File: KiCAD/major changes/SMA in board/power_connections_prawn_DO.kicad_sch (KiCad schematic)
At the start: 15 parts, among them IC1 74LVT245D,118, IC2 74LVT245D,118, IC3 74LVT245D,118, IC4 74LVT245D,118

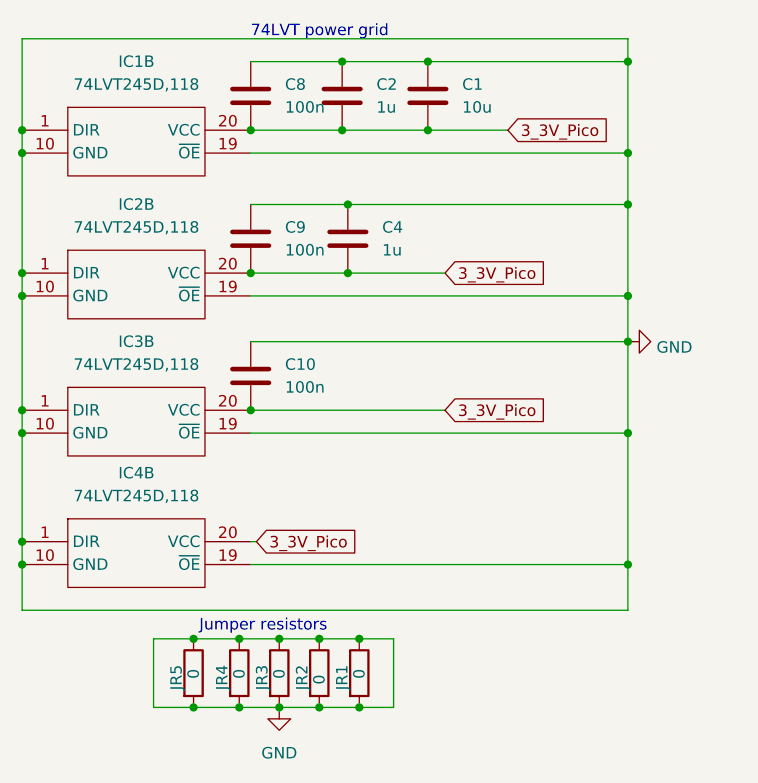
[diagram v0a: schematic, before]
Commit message: Added Mounting holes to board
Mounting holes line up with Prawnblaster.

Changed layout of components to make spacing better
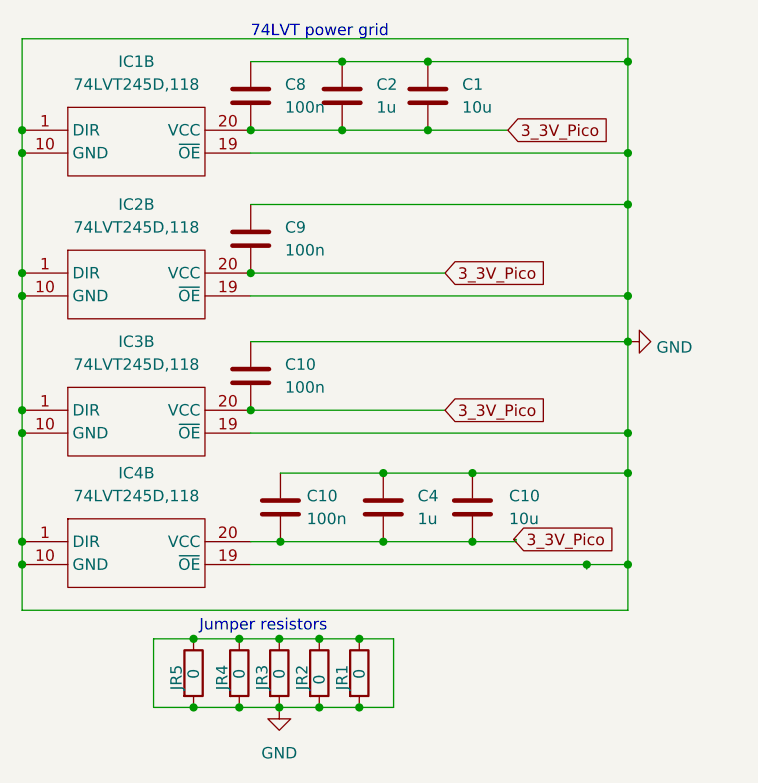
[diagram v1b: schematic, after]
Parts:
- added C10: 10u, Capacitor_SMD:C_0805_2012Metric_Pad1.18x1.45mm_HandSolder, symbol Device:C
- added C10: 100n, Capacitor_SMD:C_0805_2012Metric_Pad1.18x1.45mm_HandSolder, symbol Device:C
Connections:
- net 3_3V_Pico: now also C10.2, C10.2
- net GND: now also C10.1, C10.1
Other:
- moved on the sheet: C4
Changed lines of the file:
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@@
   (junction (at 51.435 89.535) (diameter 0) (color 0 0 0 0)
   )
-  (junction (at 59.055 41.275) (diameter 0) (color 0 0 0 0)
+  (junction (at 72.898 63.5) (diameter 0) (color 0 0 0 0)
   )
   (junction (at 67.945 17.78) (diameter 0) (color 0 0 0 0)
@@
   (junction (at 46.99 89.535) (diameter 0) (color 0 0 0 0)
   )
+  (junction (at 51.562 71.12) (diameter 0) (color 0 0 0 0)
+  )
+  (junction (at 62.992 63.5) (diameter 0) (color 0 0 0 0)
+  )
+  (junction (at 85.598 73.66) (diameter 0) (color 0 0 0 0)
+  )
   (junction (at 46.99 81.915) (diameter 0) (color 0 0 0 0)
   )
@@
   (junction (at 22.86 56.515) (diameter 0) (color 0 0 0 0)
   )
-  (junction (at 59.055 33.655) (diameter 0) (color 0 0 0 0)
-  )
   (junction (at 55.88 89.535) (diameter 0) (color 0 0 0 0)
   )
@@
   (junction (at 22.86 25.4) (diameter 0) (color 0 0 0 0)
   )
+  (junction (at 72.898 71.12) (diameter 0) (color 0 0 0 0)
+  )
   (junction (at 22.86 73.66) (diameter 0) (color 0 0 0 0)
   )
@@
   (junction (at 60.325 81.915) (diameter 0) (color 0 0 0 0)
   )
+  (junction (at 62.992 71.12) (diameter 0) (color 0 0 0 0)
+  )
   (junction (at 90.17 59.055) (diameter 0) (color 0 0 0 0)
   )
@@
   (junction (at 58.42 17.78) (diameter 0) (color 0 0 0 0)
   )
+  (junction (at 90.17 63.5) (diameter 0) (color 0 0 0 0)
+  )
   (junction (at 48.26 25.4) (diameter 0) (color 0 0 0 0)
   )
@@
     (stroke (width 0) (type default))
   )
+  (wire (pts (xy 90.17 63.5) (xy 90.17 73.66))
+    (stroke (width 0) (type default))
+  )
   (wire (pts (xy 90.17 43.815) (xy 90.17 48.895))
     (stroke (width 0) (type default))
@@
     (stroke (width 0) (type default))
   )
-  (wire (pts (xy 48.26 33.655) (xy 59.055 33.655))
+  (wire (pts (xy 48.26 33.655) (xy 90.17 33.655))
     (stroke (width 0) (type default))
   )
@@
     (stroke (width 0) (type default))
   )
+  (wire (pts (xy 72.898 63.5) (xy 90.17 63.5))
+    (stroke (width 0) (type default))
+  )
   (wire (pts (xy 55.88 81.915) (xy 60.325 81.915))
     (stroke (width 0) (type default))
@@
     (stroke (width 0) (type default))
   )
+  (wire (pts (xy 85.598 73.66) (xy 90.17 73.66))
+    (stroke (width 0) (type default))
+  )
+  (wire (pts (xy 77.724 71.12) (xy 72.898 71.12))
+    (stroke (width 0) (type default))
+  )
   (wire (pts (xy 58.42 25.4) (xy 67.945 25.4))
     (stroke (width 0) (type default))
@@
     (stroke (width 0) (type default))
   )
+  (wire (pts (xy 62.992 63.5) (xy 72.898 63.5))
+    (stroke (width 0) (type default))
+  )
   (wire (pts (xy 60.325 81.915) (xy 64.135 81.915))
     (stroke (width 0) (type default))
   )
-  (wire (pts (xy 90.17 59.055) (xy 90.17 73.66))
+  (wire (pts (xy 51.562 63.5) (xy 62.992 63.5))
+    (stroke (width 0) (type default))
+  )
+  (wire (pts (xy 72.898 71.12) (xy 62.992 71.12))
+    (stroke (width 0) (type default))
+  )
+  (wire (pts (xy 90.17 59.055) (xy 90.17 63.5))
     (stroke (width 0) (type default))
   )
@@
     (stroke (width 0) (type default))
   )
-  (wire (pts (xy 59.055 41.275) (xy 69.85 41.275))
-    (stroke (width 0) (type default))
-  )
   (wire (pts (xy 22.86 25.4) (xy 22.86 27.94))
     (stroke (width 0) (type default))
@@
     (stroke (width 0) (type default))
   )
+  (wire (pts (xy 62.992 71.12) (xy 51.562 71.12))
+    (stroke (width 0) (type default))
+  )
   (wire (pts (xy 48.26 59.055) (xy 90.17 59.055))
     (stroke (width 0) (type default))
@@
     (stroke (width 0) (type default))
   )
-  (wire (pts (xy 48.26 71.12) (xy 48.895 71.12))
+  (wire (pts (xy 77.724 70.866) (xy 77.47 70.866))
     (stroke (width 0) (type default))
   )
@@
     (stroke (width 0) (type default))
   )
-  (wire (pts (xy 48.26 41.275) (xy 59.055 41.275))
-    (stroke (width 0) (type default))
-  )
-  (wire (pts (xy 48.26 73.66) (xy 90.17 73.66))
+  (wire (pts (xy 48.26 41.275) (xy 69.85 41.275))
+    (stroke (width 0) (type default))
+  )
+  (wire (pts (xy 48.26 73.66) (xy 85.598 73.66))
+    (stroke (width 0) (type default))
+  )
+  (wire (pts (xy 51.562 71.12) (xy 48.26 71.12))
+    (stroke (width 0) (type default))
+  )
+  (wire (pts (xy 77.724 70.866) (xy 77.724 71.12))
     (stroke (width 0) (type default))
   )
@@
     (stroke (width 0) (type default))
   )
+  (wire (pts (xy 85.598 74.168) (xy 85.598 73.66))
+    (stroke (width 0) (type default))
+  )
   (wire (pts (xy 64.135 81.915) (xy 64.135 89.535))
     (stroke (width 0) (type default))
@@
   )
   (wire (pts (xy 46.99 89.535) (xy 41.91 89.535))
-    (stroke (width 0) (type default))
-  )
-  (wire (pts (xy 59.055 33.655) (xy 90.17 33.655))
     (stroke (width 0) (type default))
   )
@@
     )
   )
-  (global_label "3_3V_Pico" (shape input) (at 48.895 71.12 0) (fields_autoplaced)
+  (global_label "3_3V_Pico" (shape input) (at 77.47 70.866 0) (fields_autoplaced)
     (effects (font (size 1.27 1.27)) (justify left))
-    (property "Intersheetrefs" "${INTERSHEET_REFS}" (at 61.356 71.12 0)
+    (property "Intersheetrefs" "${INTERSHEET_REFS}" (at 89.931 70.866 0)
       (effects (font (size 1.27 1.27)) (justify left) hide)
     )
@@
     )
   )
+  (symbol (lib_id "Device:C") (at 72.898 67.31 0) (unit 1)
+    (in_bom yes) (on_board yes) (dnp no) (fields_autoplaced)
+    (property "Reference" "C10" (at 76.962 66.04 0)
+      (effects (font (size 1.27 1.27)) (justify left))
+    )
+    (property "Value" "10u" (at 76.962 68.58 0)
+      (effects (font (size 1.27 1.27)) (justify left))
+    )
+    (property "Footprint" "Capacitor_SMD:C_0805_2012Metric_Pad1.18x1.45mm_HandSolder" (at 73.8632 71.12 0)
+      (effects (font (size 1.27 1.27)) hide)
+    )
+    (property "Datasheet" "~" (at 72.898 67.31 0)
+      (effects (font (size 1.27 1.27)) hide)
+    )
+    (pin "1")
+    (pin "2")
+    (instances
+      (project "PrawnDO_Breakout_Connectorized_sma_in_board"
+        (path "/afe7a1c5-73e2-42c7-95cc-d8f50de6e194"
+          (reference "C10") (unit 1)
+        )
+        (path "/afe7a1c5-73e2-42c7-95cc-d8f50de6e194/19ec577a-8b03-4e61-8c59-aa8f06b2d188"
+          (reference "C10") (unit 1)
+        )
+      )
+    )
+  )
   (symbol (lib_id "Device:R") (at 46.99 85.725 0) (unit 1)
     (in_bom yes) (on_board yes) (dnp no)
@@
     )
   )
+  (symbol (lib_id "Device:C") (at 51.562 67.31 0) (unit 1)
+    (in_bom yes) (on_board yes) (dnp no) (fields_autoplaced)
+    (property "Reference" "C10" (at 54.483 66.04 0)
+      (effects (font (size 1.27 1.27)) (justify left))
+    )
+    (property "Value" "100n" (at 54.483 68.58 0)
+      (effects (font (size 1.27 1.27)) (justify left))
+    )
+    (property "Footprint" "Capacitor_SMD:C_0805_2012Metric_Pad1.18x1.45mm_HandSolder" (at 52.5272 71.12 0)
+      (effects (font (size 1.27 1.27)) hide)
+    )
+    (property "Datasheet" "~" (at 51.562 67.31 0)
+      (effects (font (size 1.27 1.27)) hide)
+    )
+    (pin "1")
+    (pin "2")
+    (instances
+      (project "PrawnDO_Breakout_Connectorized_sma_in_board"
+        (path "/afe7a1c5-73e2-42c7-95cc-d8f50de6e194"
+          (reference "C10") (unit 1)
+        )
+        (path "/afe7a1c5-73e2-42c7-95cc-d8f50de6e194/19ec577a-8b03-4e61-8c59-aa8f06b2d188"
+          (reference "C1") (unit 1)
+        )
+      )
+    )
+  )
   (symbol (lib_id "power:GND") (at 51.435 89.535 0) (unit 1)
     (in_bom yes) (on_board yes) (dnp no) (fields_autoplaced)
@@
     )
   )
-  (symbol (lib_id "Device:C") (at 59.055 37.465 0) (unit 1)
-    (in_bom yes) (on_board yes) (dnp no) (fields_autoplaced)
-    (property "Reference" "C4" (at 62.865 36.195 0)
-      (effects (font (size 1.27 1.27)) (justify left))
-    )
-    (property "Value" "1u" (at 62.865 38.735 0)
-      (effects (font (size 1.27 1.27)) (justify left))
-    )
-    (property "Footprint" "Capacitor_SMD:C_0805_2012Metric_Pad1.18x1.45mm_HandSolder" (at 60.0202 41.275 0)
-      (effects (font (size 1.27 1.27)) hide)
-    )
-    (property "Datasheet" "~" (at 59.055 37.465 0)
-      (effects (font (size 1.27 1.27)) hide)
-    )
+  (symbol (lib_id "Device:C") (at 62.992 67.31 0) (unit 1)
+    (in_bom yes) (on_board yes) (dnp no) (fields_autoplaced)
+    (property "Reference" "C4" (at 66.802 66.04 0)
+      (effects (font (size 1.27 1.27)) (justify left))
+    )
+    (property "Value" "1u" (at 66.802 68.58 0)
+      (effects (font (size 1.27 1.27)) (justify left))
+    )
+    (property "Footprint" "Capacitor_SMD:C_0805_2012Metric_Pad1.18x1.45mm_HandSolder" (at 63.9572 71.12 0)
+      (effects (font (size 1.27 1.27)) hide)
+    )
+    (property "Datasheet" "~" (at 62.992 67.31 0)
+      (effects (font (size 1.27 1.27)) hide)
+    )

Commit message: Moved components, added headers, changed transmission track widths, moved mounting hole placement
Changed Capacitor footprints from 0806 to 1210
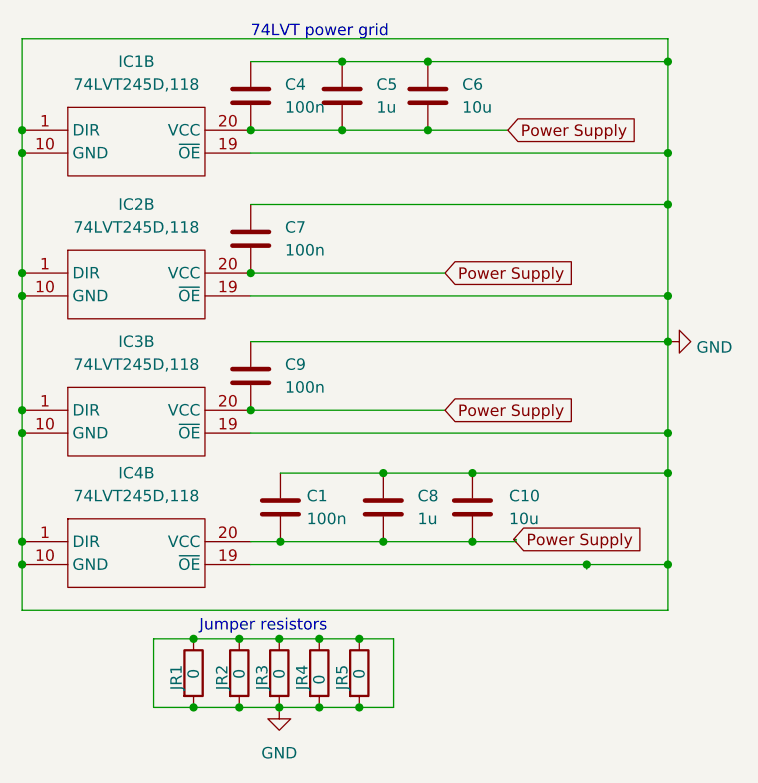
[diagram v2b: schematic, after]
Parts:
- C1, C9: renamed from C10; footprint Capacitor_SMD:C_0805_2012Metric_Pad1.18x1.45mm_HandSolder -> Capacitor_SMD:C_1210_3225Metric_Pad1.33x2.70mm_HandSolder
- C10: footprint Capacitor_SMD:C_0805_2012Metric_Pad1.18x1.45mm_HandSolder -> Capacitor_SMD:C_1210_3225Metric_Pad1.33x2.70mm_HandSolder
- C4: renamed from C8; footprint Capacitor_SMD:C_0805_2012Metric_Pad1.18x1.45mm_HandSolder -> Capacitor_SMD:C_1210_3225Metric_Pad1.33x2.70mm_HandSolder
- C5: renamed from C2; footprint Capacitor_SMD:C_0805_2012Metric_Pad1.18x1.45mm_HandSolder -> Capacitor_SMD:C_1210_3225Metric_Pad1.33x2.70mm_HandSolder
- C6: renamed from C1; footprint Capacitor_SMD:C_0805_2012Metric_Pad1.18x1.45mm_HandSolder -> Capacitor_SMD:C_1210_3225Metric_Pad1.33x2.70mm_HandSolder
- C7: renamed from C9; footprint Capacitor_SMD:C_0805_2012Metric_Pad1.18x1.45mm_HandSolder -> Capacitor_SMD:C_1210_3225Metric_Pad1.33x2.70mm_HandSolder
- C8: renamed from C4; footprint Capacitor_SMD:C_0805_2012Metric_Pad1.18x1.45mm_HandSolder -> Capacitor_SMD:C_1210_3225Metric_Pad1.33x2.70mm_HandSolder
- renumbered JR5 to JR1, JR4 to JR2, JR2 to JR4, JR1 to JR5
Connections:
- net 3_3V_Pico renamed Power  Supply

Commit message: Trace changes
Fixed some traces and added a connection to ground through pins on pico

Also made slot for USB slightly larger.

Moved resistor on bottom of board

Changed header footprint
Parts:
- C1, C10, C4, C5, C6, C7, C8, C9: footprint Capacitor_SMD:C_1210_3225Metric_Pad1.33x2.70mm_HandSolder -> Capacitor_SMD:C_1206_3216Metric_Pad1.33x1.80mm_HandSolder
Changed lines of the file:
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@@
       (effects (font (size 1.27 1.27)) (justify left))
     )
-    (property "Footprint" "Capacitor_SMD:C_1210_3225Metric_Pad1.33x2.70mm_HandSolder" (at 49.2252 56.515 0)
+    (property "Footprint" "Capacitor_SMD:C_1206_3216Metric_Pad1.33x1.80mm_HandSolder" (at 49.2252 56.515 0)
       (effects (font (size 1.27 1.27)) hide)
     )
@@
       (effects (font (size 1.27 1.27)) (justify left))
     )
-    (property "Footprint" "Capacitor_SMD:C_1210_3225Metric_Pad1.33x2.70mm_HandSolder" (at 59.3852 25.4 0)
+    (property "Footprint" "Capacitor_SMD:C_1206_3216Metric_Pad1.33x1.80mm_HandSolder" (at 59.3852 25.4 0)
       (effects (font (size 1.27 1.27)) hide)
     )
@@
       (effects (font (size 1.27 1.27)) (justify left))
     )
-    (property "Footprint" "Capacitor_SMD:C_1210_3225Metric_Pad1.33x2.70mm_HandSolder" (at 49.2252 41.275 0)
+    (property "Footprint" "Capacitor_SMD:C_1206_3216Metric_Pad1.33x1.80mm_HandSolder" (at 49.2252 41.275 0)
       (effects (font (size 1.27 1.27)) hide)
     )
@@
       (effects (font (size 1.27 1.27)) (justify left))
     )
-    (property "Footprint" "Capacitor_SMD:C_1210_3225Metric_Pad1.33x2.70mm_HandSolder" (at 73.8632 71.12 0)
+    (property "Footprint" "Capacitor_SMD:C_1206_3216Metric_Pad1.33x1.80mm_HandSolder" (at 73.8632 71.12 0)
       (effects (font (size 1.27 1.27)) hide)
     )
@@
       (effects (font (size 1.27 1.27)) (justify left))
     )
-    (property "Footprint" "Capacitor_SMD:C_1210_3225Metric_Pad1.33x2.70mm_HandSolder" (at 68.9102 25.4 0)
+    (property "Footprint" "Capacitor_SMD:C_1206_3216Metric_Pad1.33x1.80mm_HandSolder" (at 68.9102 25.4 0)
       (effects (font (size 1.27 1.27)) hide)
     )
@@
       (effects (font (size 1.27 1.27)) (justify left))
     )
-    (property "Footprint" "Capacitor_SMD:C_1210_3225Metric_Pad1.33x2.70mm_HandSolder" (at 52.5272 71.12 0)
+    (property "Footprint" "Capacitor_SMD:C_1206_3216Metric_Pad1.33x1.80mm_HandSolder" (at 52.5272 71.12 0)
       (effects (font (size 1.27 1.27)) hide)
     )
@@
       (effects (font (size 1.27 1.27)) (justify left))
     )
-    (property "Footprint" "Capacitor_SMD:C_1210_3225Metric_Pad1.33x2.70mm_HandSolder" (at 63.9572 71.12 0)
+    (property "Footprint" "Capacitor_SMD:C_1206_3216Metric_Pad1.33x1.80mm_HandSolder" (at 63.9572 71.12 0)
       (effects (font (size 1.27 1.27)) hide)
     )
@@
       (effects (font (size 1.27 1.27)) (justify left))
     )
-    (property "Footprint" "Capacitor_SMD:C_1210_3225Metric_Pad1.33x2.70mm_HandSolder" (at 49.2252 25.4 0)
-      (effects (font (size 1.27 1.27)) hide)
-    )
+    (property "Footprint" "Capacitor_SMD:C_1206_3216Metric_Pad1.33x1.80mm_HandSolder" (at 49.2252 25.4 0)
+      (effects (font (size 1.27 1.27)) hide)
+    )
